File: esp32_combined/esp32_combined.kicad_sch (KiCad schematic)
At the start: 36 parts, among them J1 HDR SKT 6PIN VERT 2.54MM, J10 HDR SKT 7PIN VERT 2.54MM, J11 HDR SKT 7PIN VERT 2.54MM, J2 HDR SKT 6PIN VERT 2.54MM, J3 HDR SKT 8PIN VERT 2.54MM, J4 TERM BLK 3.5MM 2P SIDE, J5 HDR SKT 5PIN VERT 2.54MM, J6 TERM BLK 3.5MM 4P SIDE, J7 HDR SKT 6PIN VERT 2.54MM, J8 HDR SKT 6PIN VERT 2.54MM, J9 HDR SKT 7PIN VERT 2.54MM, Q1 AS2302, SW1 SS12D10, U1 ESP32 DEV KIT Module 30-pin, U2 LM2596 Module, U3 TB6612FNG Module

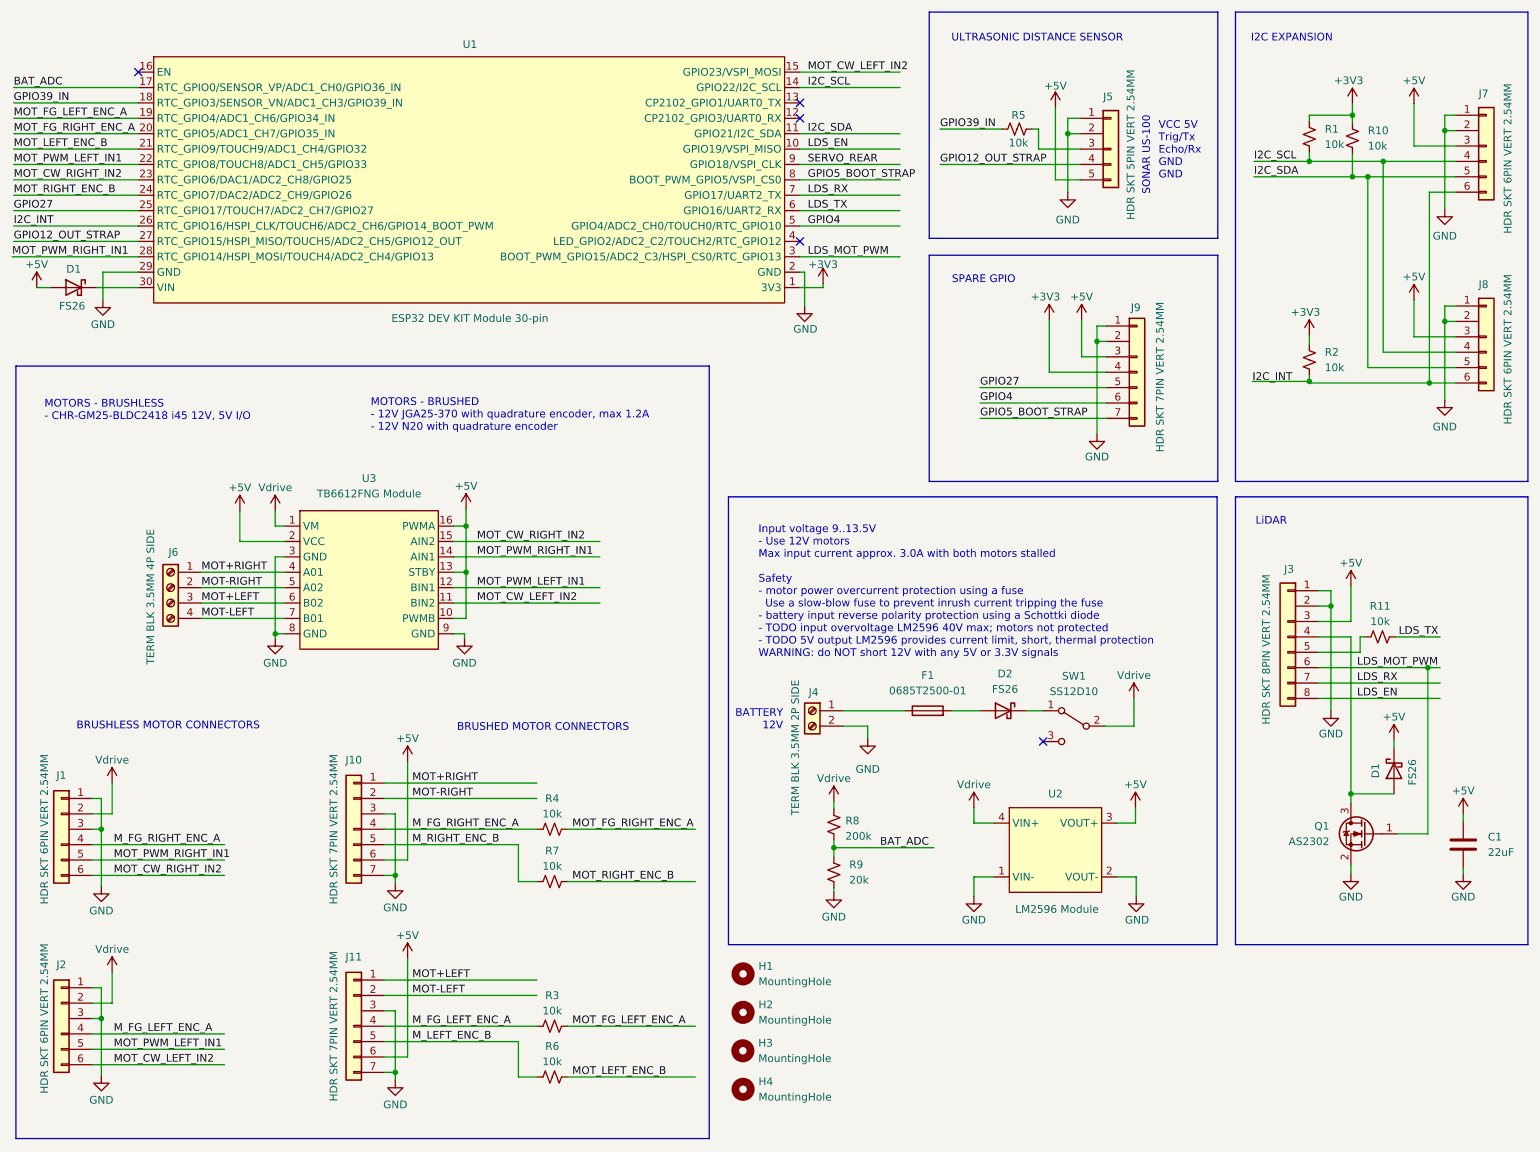
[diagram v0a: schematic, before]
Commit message: Dual headers
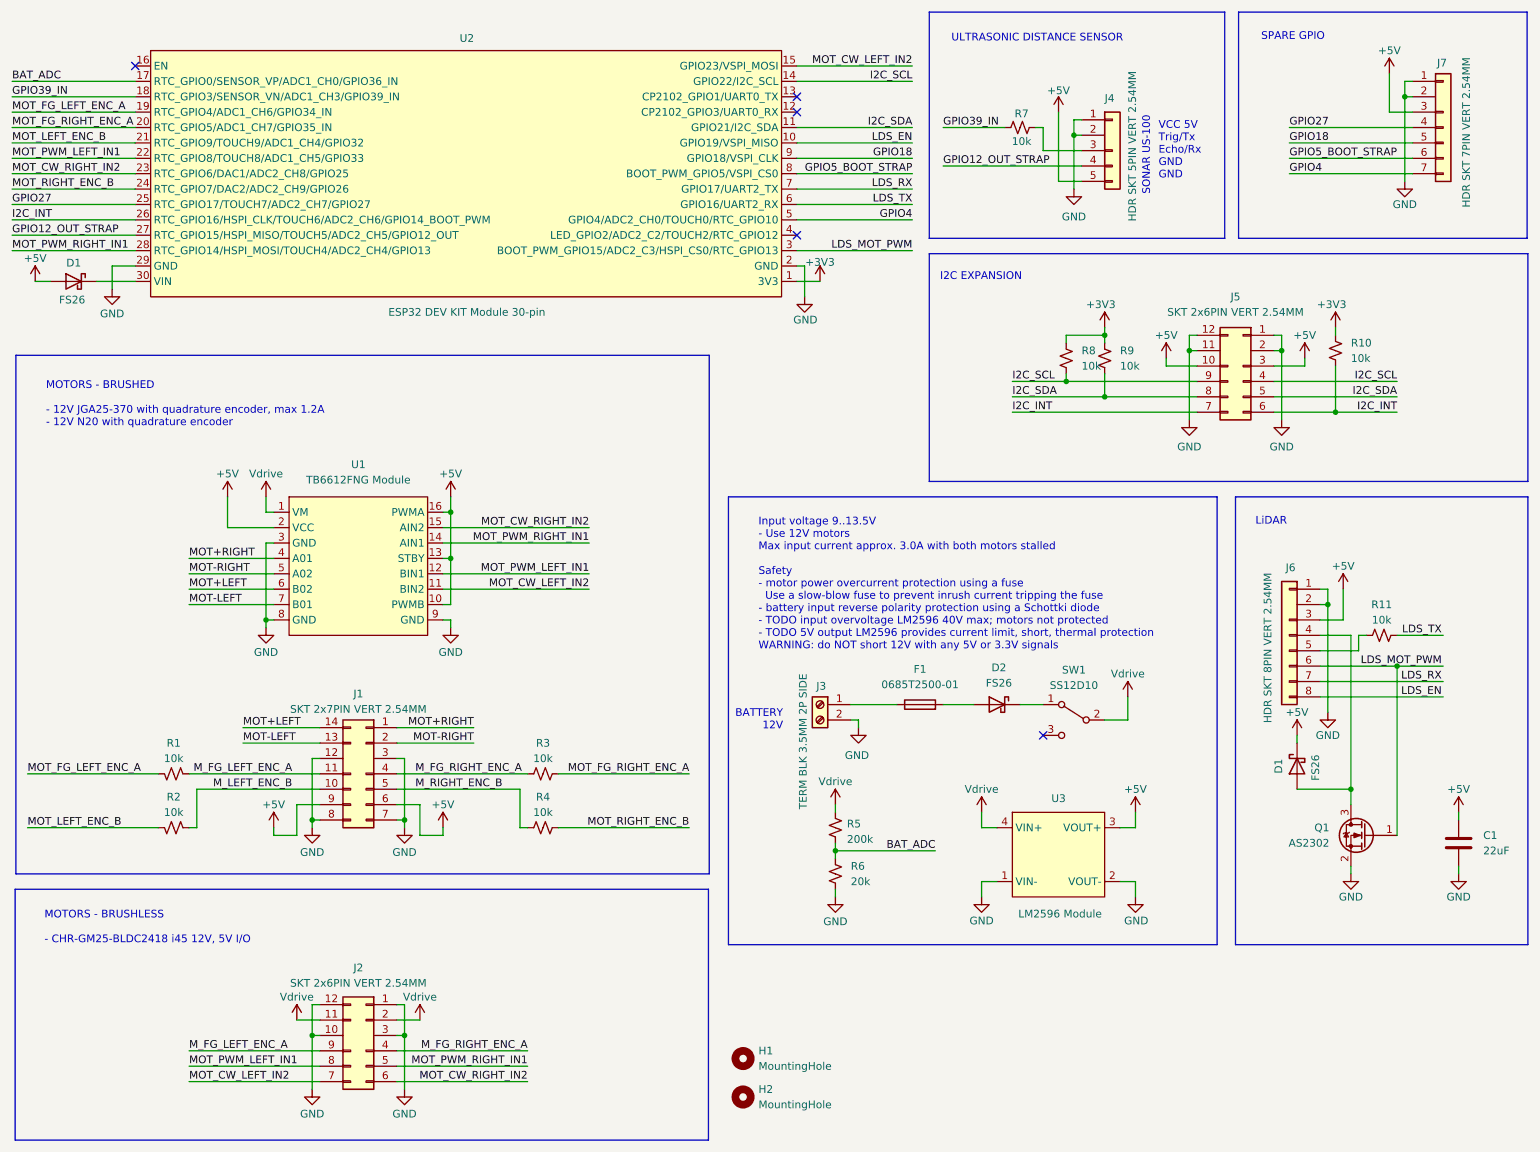
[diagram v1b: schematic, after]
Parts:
- removed H2, H4: MountingHole, MountingHole:MountingHole_3.2mm_M3, symbol Mechanical:MountingHole
- removed J1, J2: HDR SKT 6PIN VERT 2.54MM, Connector_PinSocket_2.54mm:PinSocket_1x06_P2.54mm_Vertical, symbol Makerspet:Conn_01x06_Key3
- removed J10, J11: HDR SKT 7PIN VERT 2.54MM, Connector_PinSocket_2.54mm:PinSocket_1x07_P2.54mm_Vertical, symbol Makerspet:Conn_01x07_Key3
- removed J6: TERM BLK 3.5MM 4P SIDE, symbol Connector:Screw_Terminal_01x04
- removed J7, J8: HDR SKT 6PIN VERT 2.54MM, Connector_PinSocket_2.54mm:PinSocket_1x06_P2.54mm_Vertical, symbol Makerspet:Conn_01x06_Keyed
- removed R3, R6: 10k, Resistor_SMD:R_0603_1608Metric, symbol Device:R_Small_US
- added J1: SKT 2x7PIN VERT 2.54MM, Connector_PinSocket_2.54mm:PinSocket_2x07_P2.54mm_Vertical, symbol Makerspet:Conn_02x07_Counter_Clockwise_Key3
- added J2: SKT 2x6PIN VERT 2.54MM, Connector_PinSocket_2.54mm:PinSocket_2x06_P2.54mm_Vertical, symbol Makerspet:Conn_02x06_Counter_Clockwise_Key3
- added J5: SKT 2x6PIN VERT 2.54MM, Connector_PinSocket_2.54mm:PinSocket_2x06_P2.54mm_Vertical, symbol Makerspet:Conn_02x06_Counter_Clockwise_Key2
- added R1, R2: 10k, Resistor_SMD:R_0603_1608Metric, symbol Device:R_Small_US
- J3: renamed from J4; symbol Connector:Screw_Terminal_01x02 -> Makerspet:Screw_Terminal_01x02
- J4: renamed from J5; symbol Makerspet:Conn_01x05_Keyed -> Makerspet:Conn_01x05_Key2
- J6: renamed from J3; symbol Makerspet:Conn_01x08_Keyed -> Makerspet:Conn_01x08_Key2
- J7: renamed from J9; symbol Makerspet:Conn_01x07_Keyed -> Makerspet:Conn_01x07_Key2
- U3: renamed from U2; footprint Makerspet:LM2596 Module -> Makerspet:LM2596 Module SMD; symbol Makerspet:DC-DC Module -> Makerspet:LM2596 Module
- renumbered H3 to H1, H1 to H2, R2 to R10, R4 to R3, R7 to R4, R8 to R5, R9 to R6, R5 to R7, R1 to R8, R10 to R9, U3 to U1, U1 to U2
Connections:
- net +3V3: no longer J7.4 (Pin_4)
- net +5V: now also J1.6 (Pin_6), J1.9 (Pin_9), J5.10 (Pin_10), J5.3 (Pin_3)
- net GND: now also J1.12 (Pin_12), J1.3 (Pin_3), J1.7 (Pin_7), J1.8 (Pin_8), J2.1 (Pin_1), J2.10 (Pin_10), J2.12 (Pin_12), J2.3 (Pin_3), J5.1 (Pin_1), J5.11 (Pin_11), J5.12 (Pin_12), J5.2 (Pin_2)
- net GPIO27: now also J7.4 (Pin_4); no longer J7.5 (Pin_5)
- net GPIO4: now also J7.7 (Pin_7); no longer J7.6 (Pin_6)
- net GPIO5_BOOT_STRAP: now also J7.6 (Pin_6); no longer J7.7 (Pin_7)
- net I2C_INT: now also R10.2, J5.6 (Pin_6), J5.7 (Pin_7)
- net I2C_SCL: now also J5.4 (Pin_4), J5.9 (Pin_9)
- net I2C_SDA: now also J5.5 (Pin_5), J5.8 (Pin_8)
- net MOT+LEFT: now also J1.14 (Pin_14)
- net MOT+RIGHT: now also J1.1 (Pin_1)
- net MOT-LEFT: now also J1.13 (Pin_13)
- net MOT-RIGHT: now also J1.2 (Pin_2)
- net MOT_CW_LEFT_IN2: now also J2.7 (Pin_7)
- net MOT_CW_RIGHT_IN2: now also J2.6 (Pin_6)
- net MOT_FG_LEFT_ENC_A: now also R1.1
- net MOT_LEFT_ENC_B: now also R2.1
- net MOT_PWM_LEFT_IN1: now also J2.8 (Pin_8)
- net MOT_PWM_RIGHT_IN1: now also J2.5 (Pin_5)
- net M_FG_LEFT_ENC_A: now also J1.11 (Pin_11), J2.9 (Pin_9), R1.2
- net M_FG_RIGHT_ENC_A: now also J1.4 (Pin_4), J2.4 (Pin_4)
- net M_LEFT_ENC_B: now also J1.10 (Pin_10), R2.2
- net M_RIGHT_ENC_B: now also J1.5 (Pin_5)
- net Vdrive: now also J2.11 (Pin_11), J2.2 (Pin_2)
- net SERVO_REAR renamed GPIO18
- net GPIO18: now also J7.5 (Pin_5)
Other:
- note removed: "BRUSHED MOTOR CONNECTORS"
- note removed: "BRUSHLESS MOTOR CONNECTORS"
- moved on the sheet: C1, D1, D2, F1, H1, H2, J3, J7, R10, R3, R4, R5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

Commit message: ESP32 Combined Gerber
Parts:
- removed J1: SKT 2x7PIN VERT 2.54MM, Connector_PinSocket_2.54mm:PinSocket_2x07_P2.54mm_Vertical, symbol Makerspet:Conn_02x07_Counter_Clockwise_Key3
- removed J2: SKT 2x6PIN VERT 2.54MM, Connector_PinSocket_2.54mm:PinSocket_2x06_P2.54mm_Vertical, symbol Makerspet:Conn_02x06_Counter_Clockwise_Key3
- removed J5: SKT 2x6PIN VERT 2.54MM, Connector_PinSocket_2.54mm:PinSocket_2x06_P2.54mm_Vertical, symbol Makerspet:Conn_02x06_Counter_Clockwise_Key2
- added C2: 100uF 16V, Capacitor_Tantalum_SMD:CP_EIA-7343-15_Kemet-W, symbol Device:C_Polarized_Small_US
- added H3: MountingHole, MountingHole:MountingHole_3.2mm_M3, symbol Mechanical:MountingHole
- added J1: SKT 2x7PIN VERT 2.54MM, Connector_PinSocket_2.54mm:PinSocket_2x07_P2.54mm_Vertical, symbol Makerspet:Conn_02x07_Odd_Even_Key3
- added J2: SKT 2x6PIN VERT 2.54MM, Connector_PinSocket_2.54mm:PinSocket_2x06_P2.54mm_Vertical, symbol Makerspet:Conn_02x06_Odd_Even_Key3
- added J5: SKT 2x6PIN VERT 2.54MM, Connector_PinSocket_2.54mm:PinSocket_2x06_P2.54mm_Vertical, symbol Makerspet:Conn_02x06_Odd_Even_Key2
- J6: footprint Connector_PinHeader_2.54mm:PinHeader_1x08_P2.54mm_Vertical -> Connector_PinSocket_2.54mm:PinSocket_1x08_P2.54mm_Vertical
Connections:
- net +5V: now also J1.11 (Pin_11), J1.12 (Pin_12), J5.5 (Pin_5), J5.6 (Pin_6)
- net GND: now also C2.2, J1.13 (Pin_13), J1.14 (Pin_14), J1.5 (Pin_5), J1.6 (Pin_6), J2.1 (Pin_1), J2.2 (Pin_2), J2.5 (Pin_5), J2.6 (Pin_6), J5.1 (Pin_1), J5.2 (Pin_2), J5.3 (Pin_3), J5.4 (Pin_4)
- net I2C_INT: now also J5.11 (Pin_11), J5.12 (Pin_12)
- net I2C_SCL: now also J5.7 (Pin_7), J5.8 (Pin_8)
- net I2C_SDA: now also J5.10 (Pin_10), J5.9 (Pin_9)
- net MOT+LEFT: now also J1.1 (Pin_1)
- net MOT+RIGHT: now also J1.2 (Pin_2)
- net MOT-LEFT: now also J1.3 (Pin_3)
- net MOT-RIGHT: now also J1.4 (Pin_4)
- net MOT_CW_LEFT_IN2: now also J2.11 (Pin_11)
- net MOT_CW_RIGHT_IN2: now also J2.12 (Pin_12)
- net MOT_PWM_LEFT_IN1: now also J2.9 (Pin_9)
- net MOT_PWM_RIGHT_IN1: now also J2.10 (Pin_10)
- net M_FG_LEFT_ENC_A: now also J1.7 (Pin_7), J2.7 (Pin_7)
- net M_FG_RIGHT_ENC_A: now also J1.8 (Pin_8), J2.8 (Pin_8)
- net M_LEFT_ENC_B: now also J1.9 (Pin_9)
- net M_RIGHT_ENC_B: now also J1.10 (Pin_10)
- net Vdrive: now also C2.1, J2.3 (Pin_3), J2.4 (Pin_4)
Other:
- moved on the sheet: H1, H2

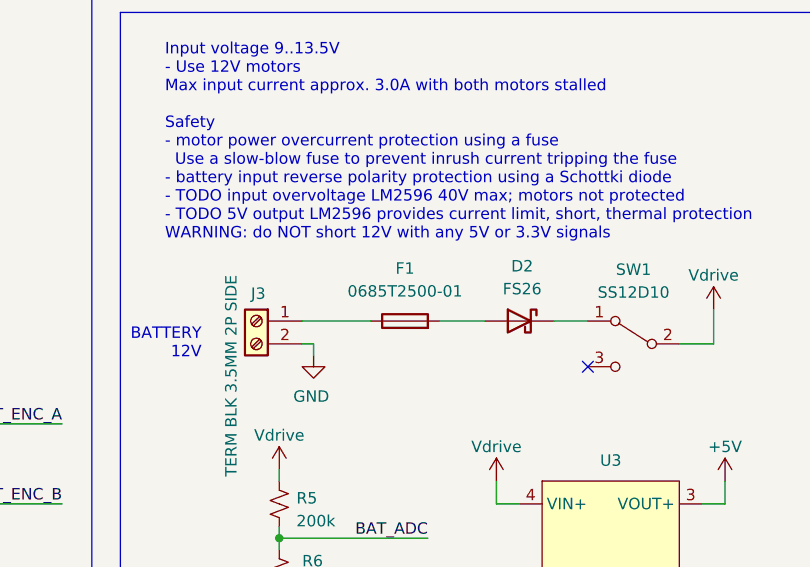
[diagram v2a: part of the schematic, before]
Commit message: Mini560 PRO DC regulator
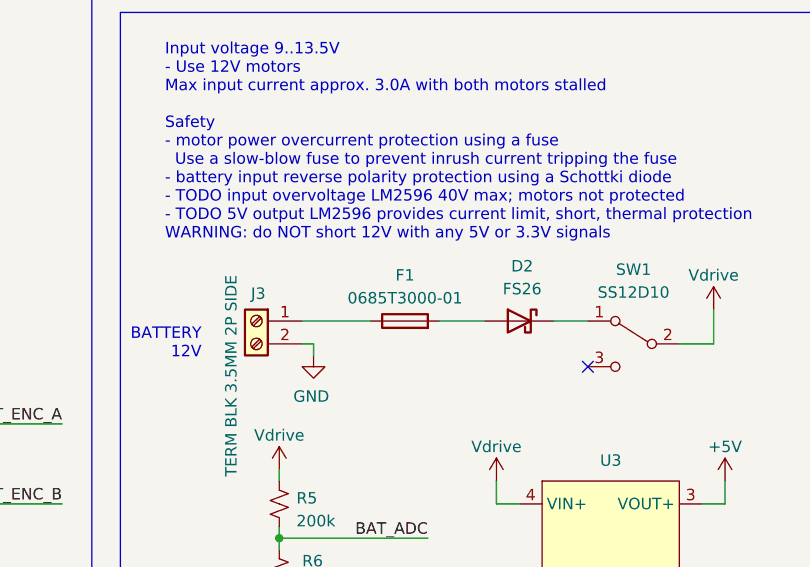
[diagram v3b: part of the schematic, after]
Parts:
- F1: value 0685T2500-01 -> 0685T3000-01
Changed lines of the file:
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@@
   (symbol (lib_id "Device:Fuse") (at 163.83 129.54 90) (unit 1)
     (in_bom yes) (on_board yes) (dnp no) (fields_autoplaced)
-    (property "Reference" "F1" (at 163.83 123.698 90)
+    (property "Reference" "F1" (at 163.83 124.46 90)
       (effects (font (size 1.27 1.27)))
     )
-    (property "Value" "0685T2500-01" (at 163.83 126.238 90)
+    (property "Value" "0685T3000-01" (at 163.83 127 90)
       (effects (font (size 1.27 1.27)))
     )
